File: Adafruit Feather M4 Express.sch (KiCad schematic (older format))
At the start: 104 parts, among them Q3 DMG341, SW1 KMR2, U1 2MB Flash, U2 AP2112-3.3, U3 MCP73831T-2ACI/OT, X1 JSTPH, X2 32.768, X3 microUSB

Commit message: Resize schematic
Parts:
- removed U$31, U$32: MOUNTINGHOLE2.5, MICROBUILDER_MOUNTINGHOLE_2.5_PLATED, symbol MICROBUILDER_MOUNTINGHOLE2.5
- removed U$34, U$35: FIDUCIAL_1MM, MICROBUILDER_FIDUCIAL_1MM, symbol MICROBUILDER_FIDUCIAL_1MM
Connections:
- net labels removed: Adafruit Industries
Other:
- moved on the sheet: C10, C11, C12, C13, C14, C15, C2, C3, C4, C5, C6, C7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

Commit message: Update BOM and add MPN to schematic parts
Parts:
- C10, C11, C12, C14, C15, C7: Count (none) -> 16; Footprint (none) -> MICROBUILDER_0603-NO; MPN (none) -> CL10B105KP8NNNC; Value (none) -> 1uF
- C13, C3, C5, C6, C8: Count (none) -> 11; Footprint (none) -> MICROBUILDER_0805-NO; MPN (none) -> C0805C106K8PACTU; Value (none) -> 10uF
- C2, C4: Count (none) -> 4; Footprint (none) -> MICROBUILDER_0603-NO; MPN (none) -> C0201C220K3GACTU; Value (none) -> 22pF
- CHG40: Count (none) -> 1; Footprint (none) -> MICROBUILDER_CHIPLED_0805_NOOUTLINE; MPN (none) -> LTST-C170KFKT; Value (none) -> ORANGE
- D+40, D-40: Count (none) -> 4; Footprint (none) -> TESTPAD_B1_27
- D4: Count (none) -> 1; Footprint (none) -> MICROBUILDER_SOD-123; MPN (none) -> MBR120VLSFT3G; Value (none) -> MBR120
- JP1: value (none) -> ~; Count (none) -> 1; Footprint (none) -> MICROBUILDER_1X16_ROUND
- JP3: value (none) -> ~; Count (none) -> 1; Footprint (none) -> MICROBUILDER_1X12_ROUND
- L2: Count (none) -> 1; Footprint (none) -> MICROBUILDER_INDUCTOR_1007; MPN (none) -> LBR2518T100K; Value (none) -> 10uH
- L40: Count (none) -> 1; Footprint (none) -> MICROBUILDER_CHIPLED_0805_NOOUTLINE; MPN (none) -> 150060RS75000; Value (none) -> RED
- LED1: Count (none) -> 1; Footprint (none) -> MICROBUILDER_LED3535; MPN (none) -> WS2812B3535; Value (none) -> WS2812B3535
- Q3: Count (none) -> 1; Footprint (none) -> MICROBUILDER_SOT23-R; MPN (none) -> DMG3413L-7; Value (none) -> DMG341
- R2: Count (none) -> 1; Footprint (none) -> MICROBUILDER_0603-NO; MPN (none) -> CRCW02011K00JNED; Value (none) -> 1K
- R3, R4, R5, R6: Count (none) -> 12; Footprint (none) -> MICROBUILDER_0603-NO; MPN (none) -> ERJ-3GEYJ103V; Value (none) -> 10K
- R7: Count (none) -> 1; Footprint (none) -> MICROBUILDER_0603-NO; MPN (none) -> ERJ-3GEYJ222V; Value (none) -> 2.2K
- R8: value (none) -> 10K; Count (none) -> 12; Footprint (none) -> MICROBUILDER_0603-NO; MPN (none) -> ERJ-3GEYJ103V; Value (none) -> 10K
- R9: Count (none) -> 1; Footprint (none) -> MICROBUILDER_RESPACK_4X0603_NO; MPN (none) -> ESR03EZPJ104; Value (none) -> 100K
- SJ1: value (none) -> ~; Count (none) -> 1; Footprint (none) -> MICROBUILDER_SOLDERJUMPER_CLOSEDWIRE
- SW1: Count (none) -> 1; Footprint (none) -> MICROBUILDER_BTN_KMR2_4.6X2.8; MPN (none) -> KMR231NG LFS; Value (none) -> KMR2
- TP1, TP2: value (none) -> ~; Count (none) -> 4; Footprint (none) -> MICROBUILDER_TESTPOINT_ROUND_1.5MM
- U$14: Count (none) -> 1; Footprint (none) -> MICROBUILDER_PQFN64-1; MPN (none) -> ATSAMD51G19A-MU; Value (none) -> ATSAMD51J
- U1: Count (none) -> 1; Footprint (none) -> MICROBUILDER_USON8; MPN (none) -> GD25Q16CTIGR; Value (none) -> 2MB Flash
- U2: Count (none) -> 1; Footprint (none) -> MICROBUILDER_SOT23-5; MPN (none) -> AP2112K-3.3TRG1; Value (none) -> AP2112-3.3
- U3: Count (none) -> 1; Footprint (none) -> MICROBUILDER_SOT23-5; MPN (none) -> MCP73831T-2ACI/OT; Value (none) -> MCP73831T-2ACI/OT
- VP_0, VP_1, VP_10, VP_11, VP_12, VP_2, VP_3, VP_4, VP_5, VP_6, VP_7, VP_8, VP_9: Count (none) -> 37; Footprint (none) -> VPAD_VPAC0
- VP_13, VP_14, VP_15, VP_16, VP_17, VP_18, VP_19, VP_20, VP_21, VP_22, VP_23, VP_24, VP_25, VP_26, VP_27, VP_31, VP_32: Count (none) -> 49; Footprint (none) -> VPAD_VPAC1
- VP_28, VP_29, VP_30, VP_33, VP_34, VP_35, VP_36, VP_37, VP_38, VP_39, VP_40, VP_41, VP_42, VP_43, VP_44, VP_45, VP_46, VP_47, VP_48, VP_49, VP_50, VP_51, VP_52, VP_53, VP_54, VP_55, VP_56, VP_57: Count (none) -> 82; Footprint (none) -> VPAD_VPAC2
- X1: Count (none) -> 1; Footprint (none) -> MICROBUILDER_JSTPH2; MPN (none) -> S2B-PH-SM4-TB(LF)(SN); Value (none) -> JSTPH
- X2: Count (none) -> 1; Footprint (none) -> ADAFRUIT2_XTAL3215; MPN (none) -> LFXTAL009678REEL; Value (none) -> 32.765
- X3: Count (none) -> 1; Footprint (none) -> MICROBUILDER_4UCONN_20329_V2; MPN (none) -> 10118194-0001LF; Value (none) -> microUSB
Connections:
- wire segments 245 -> 221

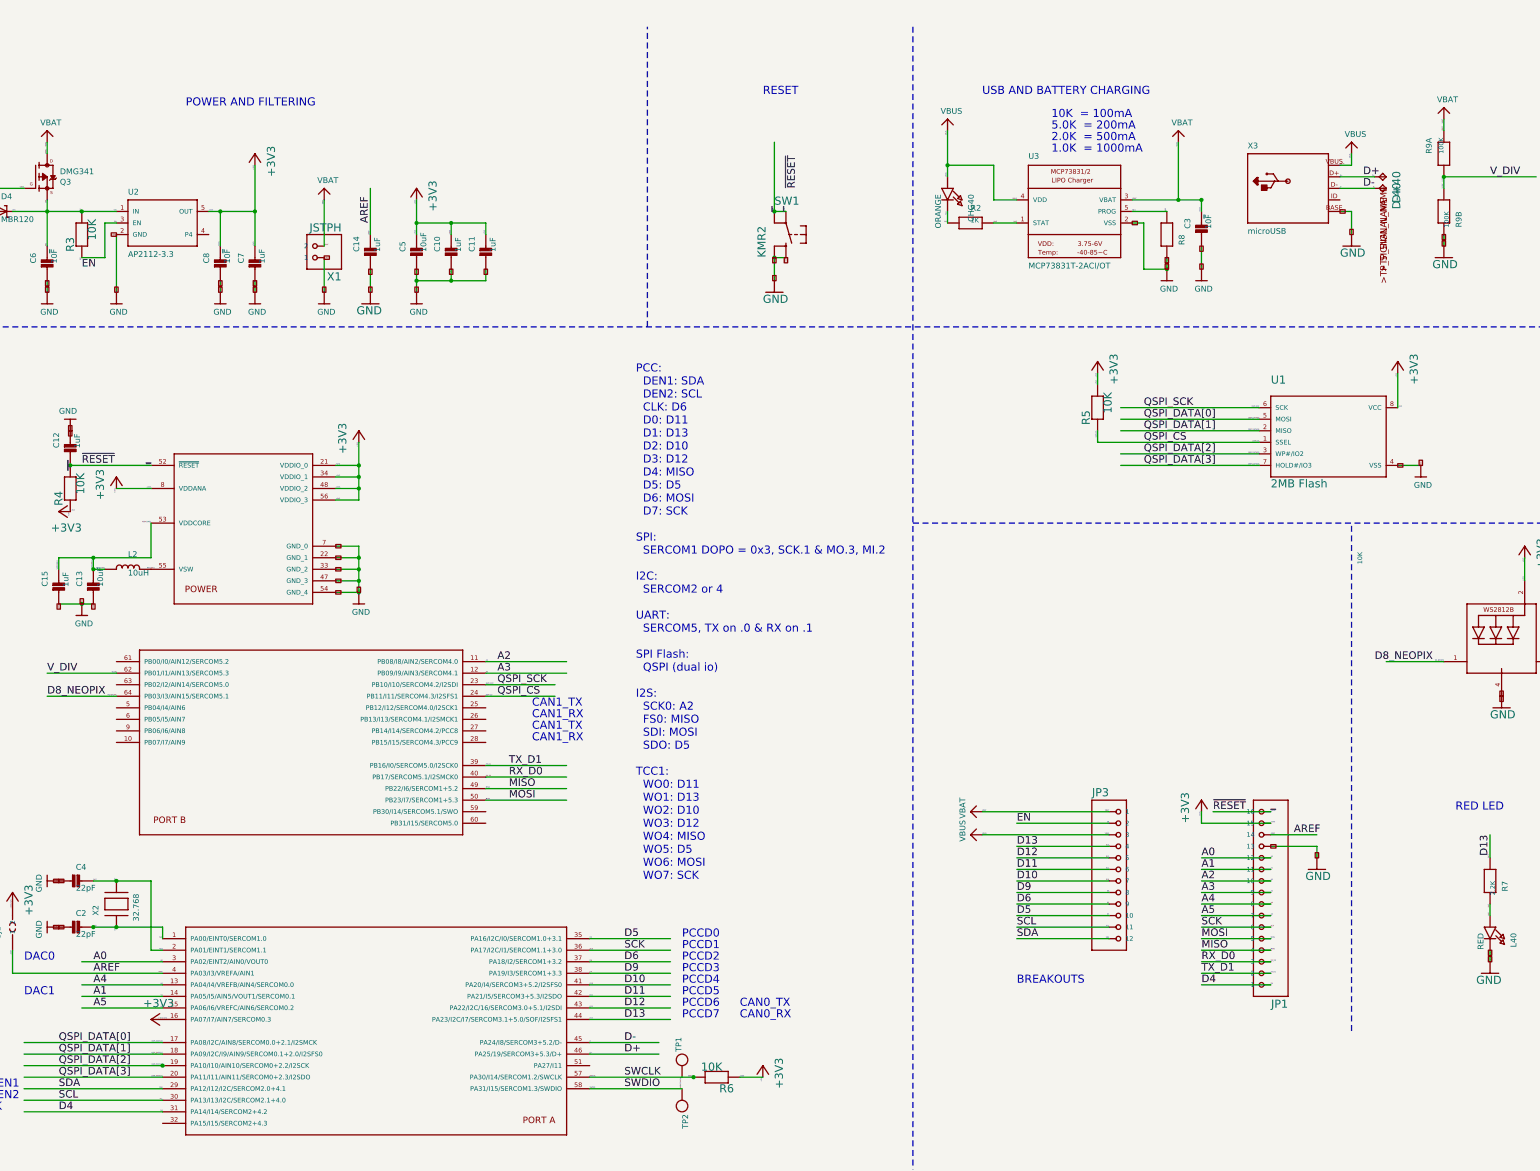
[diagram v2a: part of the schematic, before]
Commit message: Attempted to add Grove header
Got the schematic tidied up, and added Grove header to schematic.
When I went to run the footprint association it broke because the footprint file is .mod, which is legacy and not supported :(
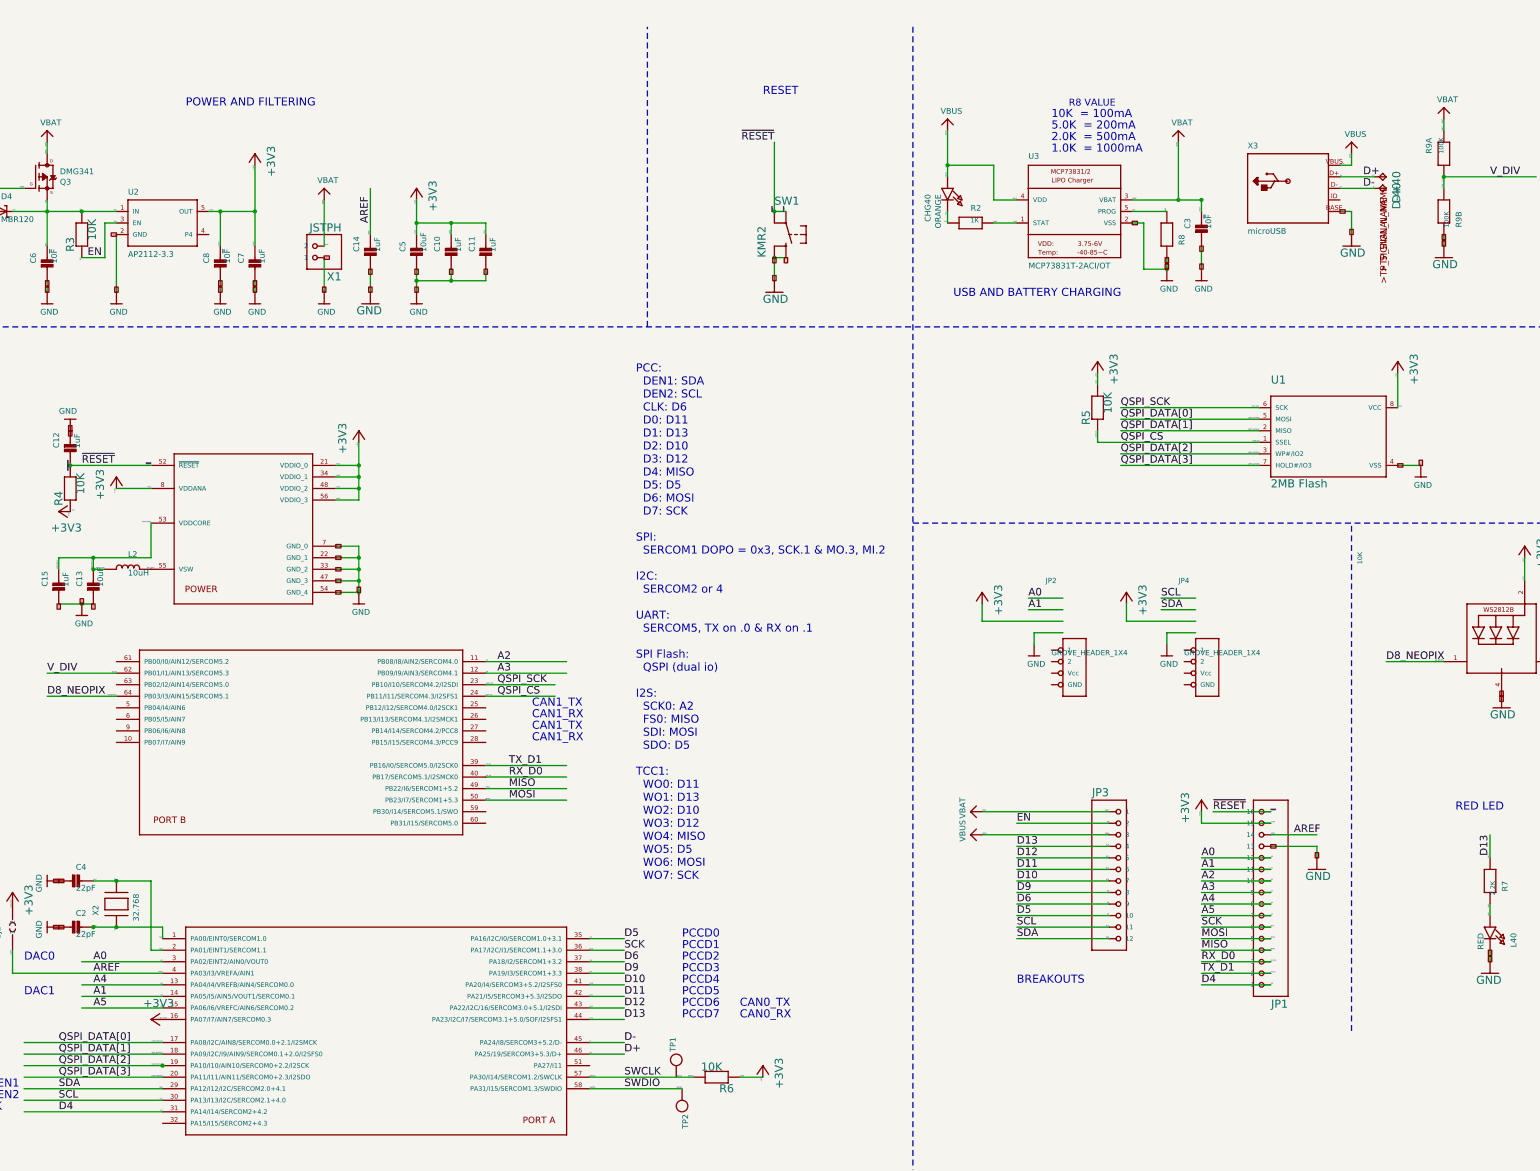
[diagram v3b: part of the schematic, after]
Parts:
- added JP2, JP4: GROVE_HEADER_1X4, GROVE_HEADER_1x4, symbol GROVE_HEADER_1X4
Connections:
- wire segments 221 -> 233
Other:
- note added: "R8 VALUE"
- moved on the sheet: TP1

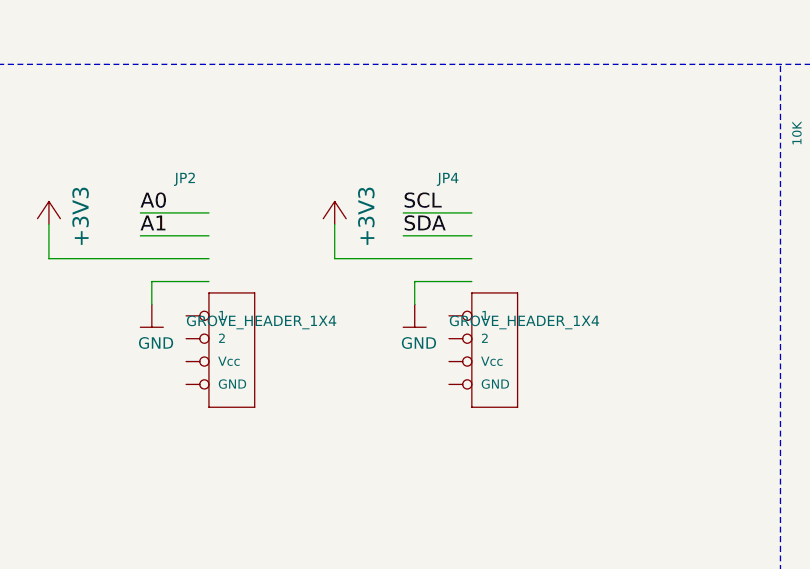
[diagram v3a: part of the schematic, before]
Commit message: Major update to board and GND pads
Added the Grove connectors.
Had to edit settings for the GND pads so that they tied to the copper pour with 'solid' instead of 'spokes' so that the pour areas would connect more. Also had to redefine the USB connector pins so that they were on the GND net. I'm getting some DRC errors that I think are erroneous, but I don't know why...
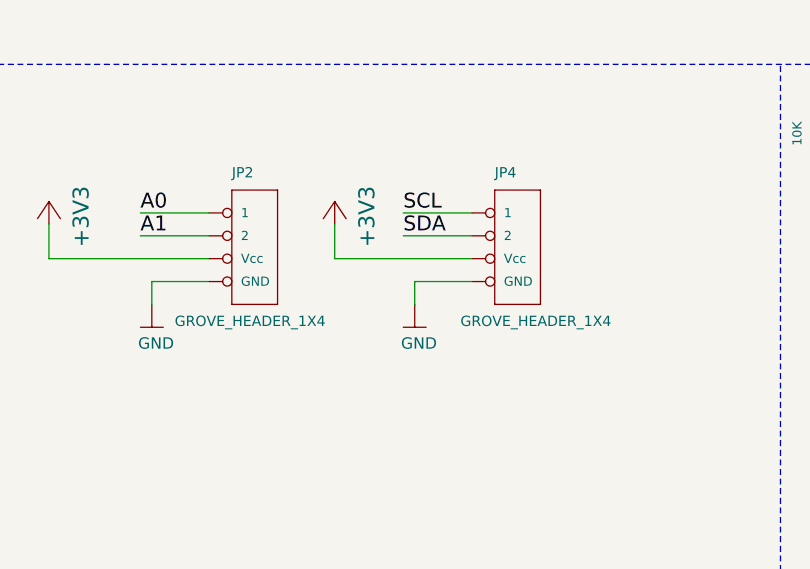
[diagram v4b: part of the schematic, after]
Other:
- moved on the sheet: JP2, JP4
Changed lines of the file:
@@
 L GROVE_HEADER_1X4 JP2
 U 1 1 5B9ACDC1
-P 11050 6550
-F 0 "JP2" H 10800 7275 45  0000 L BNN
-F 1 "GROVE_HEADER_1X4" H 10850 6650 45  0000 L BNN
-F 2 "GROVE_HEADER_1x4" H 10550 6650 20  0001 C CNN
-F 3 "" H 11050 6550 60  0000 C CNN
-	1    11050 6550
+P 11150 6100
+F 0 "JP2" H 11050 6400 45  0000 L BNN
+F 1 "GROVE_HEADER_1X4" H 10800 5750 45  0000 L BNN
+F 2 "GROVE_HEADER_1x4" H 10650 6200 20  0001 C CNN
+F 3 "" H 11150 6100 60  0000 C CNN
+	1    11150 6100
 	1    0    0    -1
 $EndComp
@@
 L GROVE_HEADER_1X4 JP4
 U 1 1 5B9ACE63
-P 12200 6550
-F 0 "JP4" H 11950 7275 45  0000 L BNN
-F 1 "GROVE_HEADER_1X4" H 12000 6650 45  0000 L BNN
-F 2 "GROVE_HEADER_1x4" H 11700 6650 20  0001 C CNN
-F 3 "" H 12200 6550 60  0000 C CNN
-	1    12200 6550
+P 12300 6100
+F 0 "JP4" H 12200 6400 45  0000 L BNN
+F 1 "GROVE_HEADER_1X4" H 12050 5750 45  0000 L BNN
+F 2 "GROVE_HEADER_1x4" H 11800 6200 20  0001 C CNN
+F 3 "" H 12300 6100 60  0000 C CNN
+	1    12300 6100
 	1    0    0    -1
 $EndComp
